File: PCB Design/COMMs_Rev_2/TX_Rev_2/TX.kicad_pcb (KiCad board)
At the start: 2 copper layers, 40 x 65 mm, 2 parts, among them J1 Conn_01x24_Pin, J2 Conn_01x24_Pin

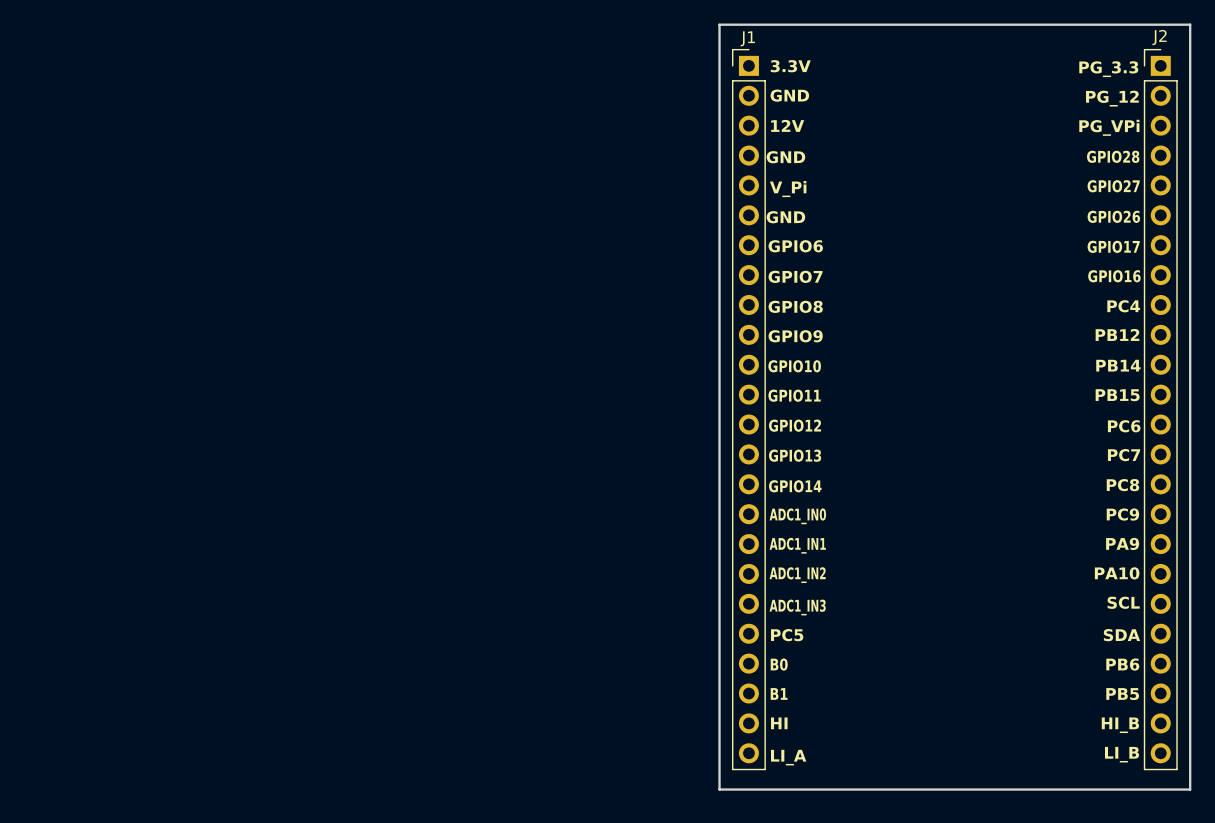
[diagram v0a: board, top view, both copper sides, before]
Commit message: Completed Initial PCB Component Placements
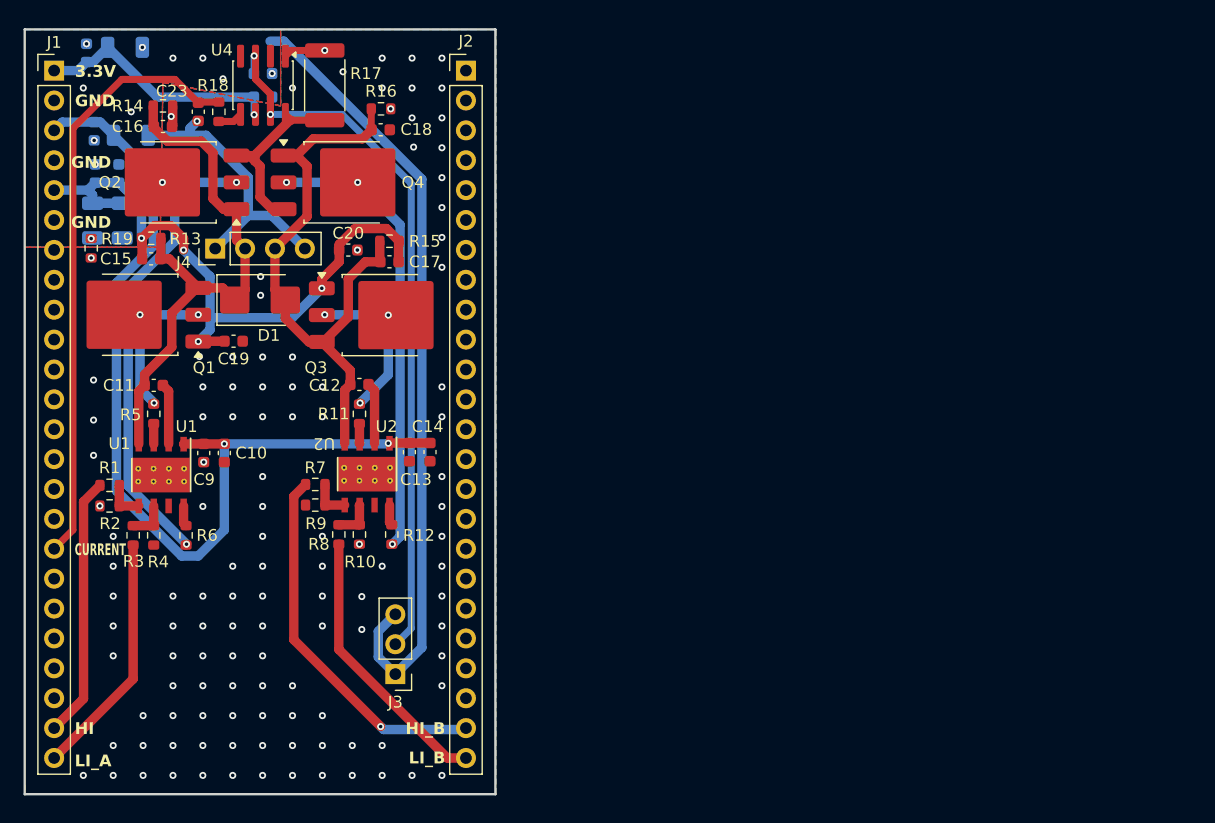
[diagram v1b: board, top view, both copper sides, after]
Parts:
- added C1: 10u, Capacitor_SMD:C_1206_3216Metric, B.Cu at (48.5, 83.2)
- added C10: 100n, Capacitor_SMD:C_0603_1608Metric, F.Cu at (59.7, 103.0)
- added C11: 100n, Capacitor_SMD:C_0603_1608Metric, F.Cu at (53.7, 97.2)
- added C12: 100n, Capacitor_SMD:C_0603_1608Metric, F.Cu at (71.2, 97.2)
- added C13: 1u, Capacitor_SMD:C_0603_1608Metric, F.Cu at (75.4, 102.9)
- added C14: 100n, Capacitor_SMD:C_0603_1608Metric, F.Cu at (77.2, 102.9)
- added C15: 1n, Capacitor_SMD:C_0603_1608Metric, F.Cu at (53.5, 86.5)
- added C16: 1n, Capacitor_SMD:C_0603_1608Metric, F.Cu at (54.5, 75.2)
- added C17: 1n, Capacitor_SMD:C_0603_1608Metric, F.Cu at (73.8, 86.8)
- added C18: 1n, Capacitor_SMD:C_0603_1608Metric, F.Cu at (73.0, 75.5)
- added C19: 100n, Capacitor_SMD:C_0603_1608Metric, F.Cu at (60.5, 93.5)
- added C2: 10u, Capacitor_SMD:C_1206_3216Metric, B.Cu at (51.0, 83.2)
- added C20: 100n, Capacitor_SMD:C_0603_1608Metric, F.Cu at (70.2, 85.8)
- added C21: 100n, Capacitor_SMD:C_0603_1608Metric, B.Cu at (63.0, 72.8)
- added C22: 100n, Capacitor_SMD:C_0603_1608Metric, B.Cu at (63.0, 70.8)
- added C23: 1n, Capacitor_SMD:C_0603_1608Metric, F.Cu at (57.5, 74.0)
- added C3: 100n, Capacitor_SMD:C_0603_1608Metric, B.Cu at (50.8, 79.2)
- added C4: 100n, Capacitor_SMD:C_0603_1608Metric, B.Cu at (48.8, 79.2)
- added C5: 10u, Capacitor_SMD:C_1206_3216Metric, B.Cu at (51.8, 76.0)
- added C6: 100n, Capacitor_SMD:C_0603_1608Metric, B.Cu at (48.7, 75.7)
- added C7: 10u, Capacitor_SMD:C_1206_3216Metric, B.Cu at (51.3, 68.5)
- added C8: 100n, Capacitor_SMD:C_0603_1608Metric, B.Cu at (48.0, 69.0)
- added C9: 1u, Capacitor_SMD:C_0603_1608Metric, F.Cu at (58.0, 103.0)
- added D1: SMBJ30A, Diode_SMD:D_SMB, F.Cu at (62.8, 90.0)
- added J3: Conn_01x03_Pin, Connector_PinHeader_2.54mm:PinHeader_1x03_P2.54mm_Vertical, F.Cu at (74.2, 121.8)
- added J4: Conn_01x04_Pin, Connector_PinHeader_2.54mm:PinHeader_1x04_P2.54mm_Vertical, F.Cu at (58.9, 85.6)
- added Q1: IPD50N10S3L16ATMA1, Package_TO_SOT_SMD:TO-252-3_TabPin2, F.Cu at (52.5, 91.2)
- added Q2: IPD50N10S3L16ATMA1, Package_TO_SOT_SMD:TO-252-3_TabPin2, F.Cu at (55.7, 80.0)
- added Q3: IPD50N10S3L16ATMA1, Package_TO_SOT_SMD:TO-252-3_TabPin2, F.Cu at (73.0, 91.3)
- added Q4: IPD50N10S3L16ATMA1, Package_TO_SOT_SMD:TO-252-3_TabPin2, F.Cu at (69.8, 80.0)
- added R1: 100, Resistor_SMD:R_0603_1608Metric, F.Cu at (50.0, 105.8)
- added R10: 100k, Resistor_SMD:R_0603_1608Metric, F.Cu at (71.2, 109.9)
- added R11: 3.3, Resistor_SMD:R_0603_1608Metric, F.Cu at (71.2, 99.7)
- added R12: 3.3, Resistor_SMD:R_0603_1608Metric, F.Cu at (73.9, 109.9)
- added R13: 6.8k, Resistor_SMD:R_0603_1608Metric, F.Cu at (53.5, 84.8)
- added R14: 6.8k, Resistor_SMD:R_0603_1608Metric, F.Cu at (54.5, 73.5)
- added R15: 6.8k, Resistor_SMD:R_0603_1608Metric, F.Cu at (73.8, 85.0)
- added R16: 6.8k, Resistor_SMD:R_0603_1608Metric, F.Cu at (73.0, 73.8)
- added R17: SHUNT, Resistor_SMD:R_2512_6332Metric, F.Cu at (68.2, 71.8)
- added R18: 10, Resistor_SMD:R_0603_1608Metric, F.Cu at (59.2, 74.0)
- added R19: 0, Resistor_SMD:R_0603_1608Metric, F.Cu at (48.4, 85.6)
- added R2: 100k, Resistor_SMD:R_0603_1608Metric, F.Cu at (50.0, 107.5)
- added R3: 100, Resistor_SMD:R_0603_1608Metric, F.Cu at (52.0, 110.0)
- added R4: 100k, Resistor_SMD:R_0603_1608Metric, F.Cu at (53.7, 110.0)
- added R5: 3.3, Resistor_SMD:R_0603_1608Metric, F.Cu at (53.7, 99.7)
- added R6: 3.3, Resistor_SMD:R_0603_1608Metric, F.Cu at (56.5, 110.0)
- added R7: 100, Resistor_SMD:R_0603_1608Metric, F.Cu at (67.4, 105.7)
- added R8: 100, Resistor_SMD:R_0603_1608Metric, F.Cu at (69.4, 109.9)
- added R9: 100k, Resistor_SMD:R_0603_1608Metric, F.Cu at (67.4, 107.4)
- added U1: UCC27211AQDDARQ1, TX:DDA0008E_L, F.Cu at (54.3, 104.9)
- added U2: UCC27211AQDDARQ1, TX:DDA0008E_L, F.Cu at (71.8, 104.8)
- added U4: INA240A2D, Package_SO:SOIC-8_3.9x4.9mm_P1.27mm, F.Cu at (63.0, 71.8)
- moved J2 59.1 mm to (80.2, 70.5)
- moved J1 59.1 mm to (45.2, 70.5)
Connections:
- J1 pad 10: /GPIO_9 -> unconnected-(J1-Pin_10-Pad10)
- J1 pad 11: /GPIO_10 -> unconnected-(J1-Pin_11-Pad11)
- J1 pad 12: /GPIO_11 -> unconnected-(J1-Pin_12-Pad12)
- J1 pad 13: /GPIO_12 -> unconnected-(J1-Pin_13-Pad13)
- J1 pad 14: /GPIO_13 -> unconnected-(J1-Pin_14-Pad14)
- J1 pad 15: /GPIO_14 -> unconnected-(J1-Pin_15-Pad15)
- J1 pad 16: /ADC1_IN0 -> unconnected-(J1-Pin_16-Pad16)
- J1 pad 17: /ADC1_IN1 -> /ADC_CURRENT
- J1 pad 18: /ADC1_IN2 -> unconnected-(J1-Pin_18-Pad18)
- J1 pad 19: /ADC1_IN3 -> unconnected-(J1-Pin_19-Pad19)
- J1 pad 20: /PC5 -> unconnected-(J1-Pin_20-Pad20)
- J1 pad 21: /PB0 -> unconnected-(J1-Pin_21-Pad21)
- J1 pad 22: /PB1 -> unconnected-(J1-Pin_22-Pad22)
- J1 pad 7: /GPIO_6 -> unconnected-(J1-Pin_7-Pad7)
- J1 pad 8: /GPIO_7 -> unconnected-(J1-Pin_8-Pad8)
- J1 pad 9: /GPIO_8 -> unconnected-(J1-Pin_9-Pad9)
- J2 pad 1: /PC3 -> unconnected-(J2-Pin_1-Pad1)
- J2 pad 10: /PB12 -> unconnected-(J2-Pin_10-Pad10)
- J2 pad 11: /PB14 -> unconnected-(J2-Pin_11-Pad11)
- J2 pad 12: /PB15 -> unconnected-(J2-Pin_12-Pad12)
- J2 pad 13: /PC6 -> unconnected-(J2-Pin_13-Pad13)
- J2 pad 14: /PC7 -> unconnected-(J2-Pin_14-Pad14)
- J2 pad 15: /PC8 -> unconnected-(J2-Pin_15-Pad15)
- J2 pad 16: /PC9 -> unconnected-(J2-Pin_16-Pad16)
- J2 pad 17: /PA9 -> unconnected-(J2-Pin_17-Pad17)
- J2 pad 18: /PA10 -> unconnected-(J2-Pin_18-Pad18)
- J2 pad 19: /SCL -> unconnected-(J2-Pin_19-Pad19)
- J2 pad 2: /PC0 -> unconnected-(J2-Pin_2-Pad2)
- J2 pad 20: /SDA -> unconnected-(J2-Pin_20-Pad20)
- J2 pad 21: /PB6 -> unconnected-(J2-Pin_21-Pad21)
- J2 pad 22: /PB5 -> unconnected-(J2-Pin_22-Pad22)
- J2 pad 3: /PC13 -> unconnected-(J2-Pin_3-Pad3)
- J2 pad 4: /GPIO_28 -> unconnected-(J2-Pin_4-Pad4)
- J2 pad 5: /GPIO_27 -> unconnected-(J2-Pin_5-Pad5)
- J2 pad 6: /GPIO_26 -> unconnected-(J2-Pin_6-Pad6)
- J2 pad 7: /GPIO_17 -> unconnected-(J2-Pin_7-Pad7)
- J2 pad 8: /GPIO_16 -> unconnected-(J2-Pin_8-Pad8)
- J2 pad 9: /PC4 -> unconnected-(J2-Pin_9-Pad9)
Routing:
- net GND: track 0.00 -> 91.8 mm, vias 0 -> 12
- net 12V: track 0.00 -> 79.3 mm, vias 0 -> 2
- net V_REF_HALF: track 0.00 -> 61.2 mm, vias 0 -> 2
- net V_Piezo: track 0.00 -> 56.9 mm, vias 0 -> 4
- net /ADC_CURRENT: track 0.00 -> 51.4 mm
- net /TX_B: track 0.00 -> 51.1 mm
- net /TX_A: track 0.00 -> 47.4 mm
- net /LO_A: track 0.00 -> 41.3 mm, vias 0 -> 3
- net /LO_B: track 0.00 -> 38.9 mm, vias 0 -> 3
- net /HI_B: track 0.00 -> 31.5 mm, vias 0 -> 1
- net /LI_B: track 0.00 -> 23.6 mm
- net /HI_A: track 0.00 -> 22.2 mm
- net 3.3V: track 0.00 -> 21.2 mm, vias 0 -> 1
- net /LI_A: track 0.00 -> 20.9 mm
- net /SHUNT_P: track 0.00 -> 15.8 mm
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- added copper zone on B.Cu, net GND
- added copper zone on F.Cu, net GND
- added copper zone on B.Cu, net HB-GND
- added copper zone on F.Cu, net HB-GND
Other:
- board text added: "CURRENT"
- board text added: "RX BOARD REV2 03/2026 By Samantha Chong"
- board text removed: "12V"
- board text removed: "ADC1_IN0"
- board text removed: "ADC1_IN1"
- board text removed: "ADC1_IN2"
- board text removed: "ADC1_IN3"
- board text removed: "B0"
- board text removed: "B1"
- board text removed: "GPIO10"
- board text removed: "GPIO11"
- board text removed: "GPIO12"
- board text removed: "GPIO13"
- board text removed: "GPIO14"
- board text removed: "GPIO16"
- board text removed: "GPIO17"
- board text removed: "GPIO26"
- board text removed: "GPIO27"
- board text removed: "GPIO28"
- board text removed: "GPIO6"
- board text removed: "GPIO7"
- board text removed: "GPIO8"
- board text removed: "GPIO9"
- board text removed: "PA10"
- board text removed: "PA9"
- board text removed: "PB12"
- board text removed: "PB14"
- board text removed: "PB15"
- board text removed: "PB5"
- board text removed: "PB6"
- board text removed: "PC4"
- board text removed: "PC5"
- board text removed: "PC6"
- board text removed: "PC7"
- board text removed: "PC8"
- board text removed: "PC9"
- board text removed: "PG_12"
- board text removed: "PG_3.3"
- board text removed: "PG_VPi"
- board text removed: "SCL"
- board text removed: "SDA"
- board text removed: "TX BOARD REV2 03/2026 By Samantha Chong"
- board text removed: "V_Pi"

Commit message: Updated Revision Number and Title Block
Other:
- board text added: "RX BOARD REV2.1 03/2026 By Samantha Chong"
- board text removed: "RX BOARD REV2 03/2026 By Samantha Chong"
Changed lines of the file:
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@@
 			)
 			(layer "F.SilkS")
-			(net 6619240)
 		)
 		(fp_line
@@
 			)
 			(layer "F.SilkS")
-			(net 6619240)
 		)
 		(fp_line
@@
 			)
 			(layer "F.SilkS")
-			(net 6619240)
 		)
 		(fp_line
@@
 			)
 			(layer "F.SilkS")
-			(net 6619240)
 		)
 		(fp_line
@@
 			)
 			(layer "F.SilkS")
-			(net 6619240)
 		)
 		(fp_line
@@
 			)
 			(layer "F.SilkS")
-			(net 6619240)
 		)
 		(fp_line
@@
 			)
 			(layer "F.CrtYd")
-			(net 6619240)
 		)
 		(fp_line
@@
 			)
 			(layer "F.CrtYd")
-			(net 6619240)
 		)
 		(fp_line
@@
 			)
 			(layer "F.CrtYd")
-			(net 6619240)
 		)
 		(fp_line
@@
 			)
 			(layer "F.CrtYd")
-			(net 6619240)
 		)
 		(fp_line
@@
 			)
 			(layer "F.Fab")
-			(net 6619240)
 		)
 		(fp_line
@@
 			)
 			(layer "F.Fab")
-			(net 6619240)
 		)
 		(fp_line
@@
 			)
 			(layer "F.Fab")
-			(net 6619240)
 		)
 		(fp_line
@@
 			)
 			(layer "F.Fab")
-			(net 6619240)
 		)
 		(fp_line
@@
 			)
 			(layer "F.Fab")
-			(net 6619240)
 		)
 		(pad "1" thru_hole rect
@@
 			)
 			(layer "F.SilkS")
-			(net 6619240)
 		)
 		(fp_line
@@
 			)
 			(layer "F.SilkS")
-			(net 6619240)
 		)
 		(fp_line
@@
 			)
 			(layer "F.SilkS")
-			(net 6619240)
 		)
 		(fp_line
@@
 			)
 			(layer "F.SilkS")
-			(net 6619240)
 		)
 		(fp_line
@@
 			)
 			(layer "F.SilkS")
-			(net 6619240)
 		)
 		(fp_line
@@
 			)
 			(layer "F.SilkS")
-			(net 6619240)
 		)
 		(fp_line
@@
 			)
 			(layer "F.CrtYd")
-			(net 6619240)
 		)
 		(fp_line
@@
 			)
 			(layer "F.CrtYd")
-			(net 6619240)
 		)
 		(fp_line
@@
 			)
 			(layer "F.CrtYd")
-			(net 6619240)
 		)
 		(fp_line
@@
 			)
 			(layer "F.CrtYd")
-			(net 6619240)
 		)
 		(fp_line
@@
 			)
 			(layer "F.Fab")
-			(net 6619240)
 		)
 		(fp_line
@@
 			)
 			(layer "F.Fab")
-			(net 6619240)
 		)
 		(fp_line
@@
 			)
 			(layer "F.Fab")
-			(net 6619240)
 		)
 		(fp_line
@@
 			)
 			(layer "F.Fab")
-			(net 6619240)
 		)
 		(fp_line
@@
 			)
 			(layer "F.Fab")
-			(net 6619240)
 		)
 		(pad "1" thru_hole rect
@@
 			)
 			(layer "F.SilkS")
-			(net 6619240)
 		)
 		(fp_line
@@
 			)
 			(layer "F.SilkS")
-			(net 6619240)
 		)
 		(fp_line
@@
 			)
 			(layer "F.SilkS")
-			(net 6619240)
 		)
 		(fp_line
@@
 			)
 			(layer "F.SilkS")
-			(net 6619240)
 		)
 		(fp_line
@@
 			)
 			(layer "F.SilkS")
-			(net 6619240)
 		)
 		(fp_line
@@
 			)
 			(layer "F.SilkS")
-			(net 6619240)
 		)
 		(fp_line
@@
 			)
 			(layer "F.CrtYd")
-			(net 6619240)
 		)
 		(fp_line
@@
 			)
 			(layer "F.CrtYd")
-			(net 6619240)
 		)
 		(fp_line
@@
 			)
 			(layer "F.CrtYd")
-			(net 6619240)
 		)
 		(fp_line
@@
 			)
 			(layer "F.CrtYd")
-			(net 6619240)
 		)
 		(fp_line
@@
 			)
 			(layer "F.Fab")
-			(net 6619240)
 		)
 		(fp_line
@@
 			)
 			(layer "F.Fab")
-			(net 6619240)
 		)
 		(fp_line
@@
 			)
 			(layer "F.Fab")
-			(net 6619240)
 		)
 		(fp_line
@@
 			)
 			(layer "F.Fab")
-			(net 6619240)
 		)
 		(fp_line
@@
 			)
 			(layer "F.Fab")
-			(net 6619240)
 		)
 		(fp_text user "${REFERENCE}"
@@
 			)
 			(layer "F.SilkS")
-			(net 6619240)
 		)
 		(fp_line
@@
 			)
 			(layer "F.SilkS")
-			(net 6619240)
 		)
 		(fp_line
@@
 			)
 			(layer "F.SilkS")
-			(net 6619240)
 		)
 		(fp_line
@@
 			)
 			(layer "F.SilkS")
-			(net 6619240)
 		)
 		(fp_line
@@
 			)
 			(layer "F.SilkS")
-			(net 6619240)
 		)
 		(fp_line
@@
 			)
 			(layer "F.SilkS")
-			(net 6619240)
 		)
 		(fp_line
@@
 			)
 			(layer "F.CrtYd")
-			(net 6619240)
 		)
 		(fp_line
@@
 			)
 			(layer "F.CrtYd")
-			(net 6619240)
 		)
 		(fp_line
@@
 			)
 			(layer "F.CrtYd")
-			(net 6619240)
 		)
 		(fp_line
@@
 			)
 			(layer "F.CrtYd")
-			(net 6619240)
 		)
 		(fp_line
@@
 			)
 			(layer "F.Fab")
-			(net 6619240)
 		)
 		(fp_line
@@
 			)
 			(layer "F.Fab")
-			(net 6619240)
 		)
 		(fp_line
@@
 			)
 			(layer "F.Fab")
-			(net 6619240)
 		)
 		(fp_line
@@
 			)
 			(layer "F.Fab")
-			(net 6619240)
 		)
 		(fp_line
@@
 			)
 			(layer "F.Fab")
-			(net 6619240)
 		)
 		(fp_text user "${REFERENCE}"
@@
 		)
 	)
-	(gr_text "RX BOARD \nREV2 03/2026\nBy Samantha Chong"
+	(gr_text "RX BOARD \nREV2.1 03/2026\nBy Samantha Chong"
 		(at 66.15 130.8 0)
 		(layer "B.SilkS")

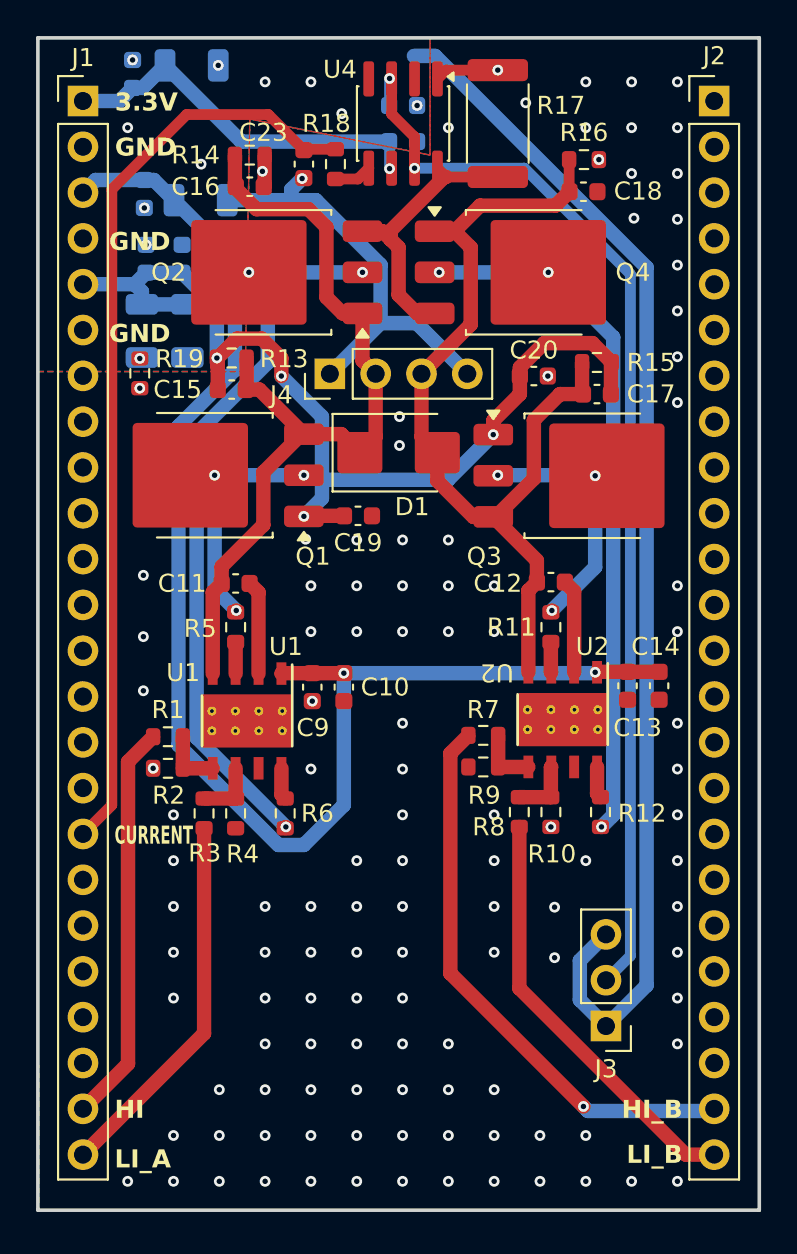
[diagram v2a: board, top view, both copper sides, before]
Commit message: Updated Schematic to include Inductor Matching Inductors
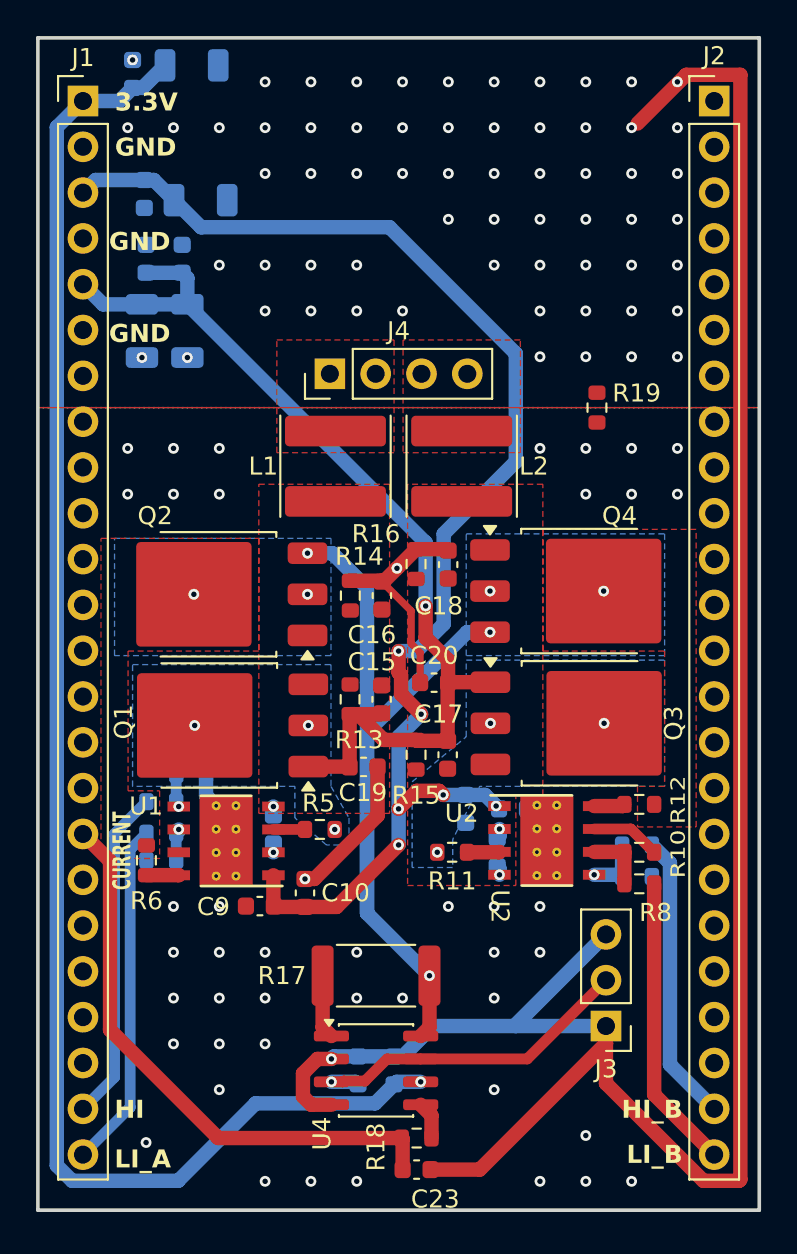
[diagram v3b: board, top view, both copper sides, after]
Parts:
- removed D1: SMBJ30A, Diode_SMD:D_SMB
- added L1: L, Inductor_SMD:L_Wuerth_MAPI-5030, F.Cu at (59.2, 90.8)
- added L2: L, Inductor_SMD:L_Wuerth_MAPI-5030, F.Cu at (66.2, 90.8)
- C11, C12, C13, C14, R1, R2, R3, R4, R7, R9: moved to B.Cu
- R11, R12, R5, R6: value 3.3 -> 10
- moved C23 56.1 mm to (63.8, 129.8), turned to 0 degrees
- moved R18 54.2 mm to (63.8, 128.0), turned to 180 degrees
- moved C22 53.6 mm to (60.5, 124.2), turned to 90 degrees
- moved U4 52.5 mm to (61.5, 124.2), turned to 0 degrees
- moved C21 51.5 mm to (62.5, 124.2), turned to 90 degrees
- moved R17 47.7 mm to (61.5, 119.0), turned to 180 degrees
- moved R19 25.4 mm to (73.8, 87.5)
- moved R14 25.1 mm to (60.1, 97.9), turned to 90 degrees
- moved R16 24.3 mm to (63.7, 96.2), turned to 90 degrees
- moved R15 24.0 mm to (63.7, 106.8), turned to -90 degrees
- moved C16 23.8 mm to (61.8, 97.9), turned to 90 degrees
- moved C18 22.0 mm to (65.5, 96.2), turned to 90 degrees
- moved C17 21.6 mm to (65.5, 106.8), turned to -90 degrees
- moved R13 20.0 mm to (60.1, 103.7), turned to 90 degrees
- moved C15 19.1 mm to (61.8, 103.7), turned to 90 degrees
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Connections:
- C11 pad 2: /TX_A -> /H_A
- C12 pad 2: /TX_B -> /H_B
- C15 pad 2: /TX_A -> /H_A
- C16 pad 1: /TX_A -> /H_A
- C17 pad 2: /TX_B -> /H_B
- C18 pad 1: /TX_B -> /H_B
- Q1 pad 3: /TX_A -> /H_A
- Q2 pad 1: /TX_A -> /H_A
- Q3 pad 3: /TX_B -> /H_B
- Q4 pad 1: /TX_B -> /H_B
- R13 pad 2: /TX_A -> /H_A
- R14 pad 1: /TX_A -> /H_A
- R15 pad 2: /TX_B -> /H_B
- R16 pad 1: /TX_B -> /H_B
- U1 pad 4: /TX_A -> /H_A
- U2 pad 4: /TX_B -> /H_B
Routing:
- net 3.3V: track 21.2 -> 87.8 mm
- net /TX_B: track 51.1 -> 0.00 mm
- net /TX_A: track 47.4 -> 0.00 mm
- net V_REF_HALF: track 61.2 -> 19.1 mm, vias 2 -> 1
- net /LO_A: track 41.3 -> 0.00 mm, vias 3 -> 2
- net /LO_B: track 38.9 -> 0.00 mm, vias 3 -> 2
- net /SHUNT_P: track 15.8 -> 49.7 mm, vias 0 -> 3
- net GND: track 91.8 -> 121.7 mm, vias 12 -> 64
- net HB-GND: track 5.32 -> 30.2 mm, vias 118 -> 45
- net /ADC_CURRENT: track 51.4 -> 31.9 mm
- net /HI_B: track 31.5 -> 16.1 mm, vias 1 -> 0
- net /HO_B: track 14.3 -> 0.00 mm
- net /HO_A: track 13.1 -> 0.00 mm
- net /LI_B: track 23.6 -> 16.4 mm
- net Net-(U1-HB): track 5.21 -> 0.50 mm, vias 0 -> 1
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- added copper zone on B.Cu, net /HO_A
- added copper zone on B.Cu, net /HO_B
- added copper zone on F.Cu, net /H_A
- added copper zone on F.Cu, net /H_B
- added copper zone on B.Cu, net /LO_A
- added copper zone on F.Cu, net /LO_A
- added copper zone on B.Cu, net /LO_B
- added copper zone on F.Cu, net /LO_B
- added copper zone on F.Cu, net /TX_A
- added copper zone on F.Cu, net /TX_B
